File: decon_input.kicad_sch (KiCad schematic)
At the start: 35 parts, among them J21 Conn_01x02, U1 LTV-817S, U2 LTV-817S, U22 LTV-817S, U23 LTV-817S, U24 LTV-817S, U25 LTV-817S, U4 LTV-817S, U5 LTV-817S

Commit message: modified:   DECON_Ctrl_Panel.kicad_pcb 	modified:   DECON_Ctrl_Panel.kicad_prl 	new file:   MCU_pins.xlsx 	new file:   Son_KiCad_lib/Son_KiCad_lib.bak 	new file:   Son_KiCad_lib/Son_KiCad_lib.kicad_sym 	new file:   Son_KiCad_lib/Son_KiCad_lib.pretty/URB2405YMD-10WR3.kicad_mod 	modified:   decon_input.kicad_sch 	modified:   decon_mcu.kicad_sch 	modified:   decon_output.kicad_sch 	modified:   decon_power.kicad_sch 	new file:   fp-lib-table 	new file:   sym-lib-table
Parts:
- removed D1, D2, D3, D4, D41, D5, D6, D7: LED, LED_SMD:LED_0805_2012Metric, symbol Device:LED
- removed J21: Conn_01x02, TerminalBlock_Phoenix:TerminalBlock_Phoenix_MKDS-1-2-3.81_1x02_P3.81mm_Horizontal, symbol Connector_Generic:Conn_01x02
- removed R1, R3, R41, R45, R5, R7: 1K, Resistor_SMD:R_0805_2012Metric, symbol Device:R
- removed R2, R4, R42, R46, R6, R8: 10K, Resistor_SMD:R_0805_2012Metric, symbol Device:R
- removed U1, U2, U22, U23, U24, U25, U4, U5: LTV-817S, Package_DIP:SMDIP-4_W9.53mm, symbol Isolator:LTV-817S
- added J21, J22: Conn_01x10, Connector_Phoenix_MC:PhoenixContact_MC_1,5_10-G-3.81_1x10_P3.81mm_Horizontal, symbol Connector_Generic:Conn_01x10
- added R51, R52, R53, R54, R71, R72, R73, R74, R75, R76: 1K, Resistor_SMD:R_0805_2012Metric, symbol Device:R
- added R65, R66, R67, R68, R69, R70, R77, R78, R79, R80, R81, R82, R83, R84, R85, R86, R87, R88, R89: 10K, Resistor_SMD:R_0805_2012Metric, symbol Device:R
- added U2: 74HC138, Package_SO:SOIC-16_3.9x9.9mm_P1.27mm, symbol 74xx:74HC138
- added U26, U27, U34, U35, U36, U37, U38, U39: LTV-817S, Package_DIP:SMDIP-4_W9.53mm, symbol Isolator:LTV-817S
- R48, R50: value 10K -> 1K
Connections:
- net 24V is gone; now on net 3.3V: R43.1
- net BUTTON_1 is gone; now on net 3.3V: R47.1, R49.1
- net 3.3V: now also R44.1, R51.1, R53.1, R65.2, R66.2, R67.2, R68.2, R69.2, R70.2, R77.2, R78.2, R79.2, R80.2, R81.2, R82.2, R83.2, R84.2, R85.2, R86.2, R87.2, R88.2, R89.2, U2.16 (VCC), U2.6 (E2)
- net at R47.2: now also U34.1
- net at R49.2: now also U36.1
- net at R48.2: now also U35.1
- net at R43.2: now also U26.1; no longer R44.1
- net at R50.2: now also U37.1
- net GND_24V: no longer names the net of R44.2
- net GND_24V: now also U27.1
- new net: R52.1, U26.4
- new net: R71.1, U34.4
- new net: R51.2, U38.1
- new net: R53.2, U39.1
- new net: R76.1, U39.4
- new net: R73.1, U36.4
- new net: R54.1, U27.4
- new net: R72.1, U35.4
- new net: R74.1, U37.4
- new net: R75.1, U38.4
- new net 74138_Y0: R65.1, R89.1, U2.15 (~{Y0}), U2.3 (A2), U26.2
- new net 74138_Y1: R66.1, R88.1, U2.14 (~{Y1}), U2.2 (A1), U34.2
- new net 74138_Y2: R67.1, R87.1, U2.1 (A0), U2.13 (~{Y2}), U35.2
- new net 74138_Y3: R68.1, U2.12 (~{Y3}), U36.2
- new net 74138_Y4: R69.1, U2.11 (~{Y4}), U27.2
- new net 74138_Y5: R70.1, U2.10 (~{Y5}), U37.2
- new net 74138_Y6: R77.1, U2.9 (~{Y6}), U38.2
- new net 74138_Y7: R78.1, U2.7 (~{Y7}), U39.2
- new net GND_MCU: J21.1 (Pin_1), J21.10 (Pin_10), U2.4 (~{E0}), U2.5 (~{E1}), U2.8 (GND)
- new net GND_VBAT: J22.1 (Pin_1), J22.10 (Pin_10)
- new net LED_0: U26.3
- new net LED_1: J22.2 (Pin_2), U34.3
- new net LED_2: J22.3 (Pin_3), U35.3
- new net LED_3: J22.4 (Pin_4), U36.3
- new net LED_4: J22.5 (Pin_5), U27.3
- new net LED_5: J22.6 (Pin_6), U37.3
- new net LED_6: J22.7 (Pin_7), U38.3
- new net LED_7: J22.8 (Pin_8), U39.3
- new net LED_8: J22.9 (Pin_9)
- new net MCU_BTN_0: J21.2 (Pin_2), R86.1
- new net MCU_BTN_1: J21.3 (Pin_3), R85.1
- new net MCU_BTN_2: J21.4 (Pin_4), R84.1
- new net MCU_BTN_3: J21.5 (Pin_5), R83.1
- new net MCU_BTN_4: J21.6 (Pin_6), R82.1
- new net MCU_BTN_5: J21.7 (Pin_7), R81.1
- new net MCU_BTN_6: J21.8 (Pin_8), R80.1
- new net MCU_BTN_7: J21.9 (Pin_9), R79.1
- new net VBAT: R52.2, R54.2, R71.2, R72.2, R73.2, R74.2, R75.2, R76.2

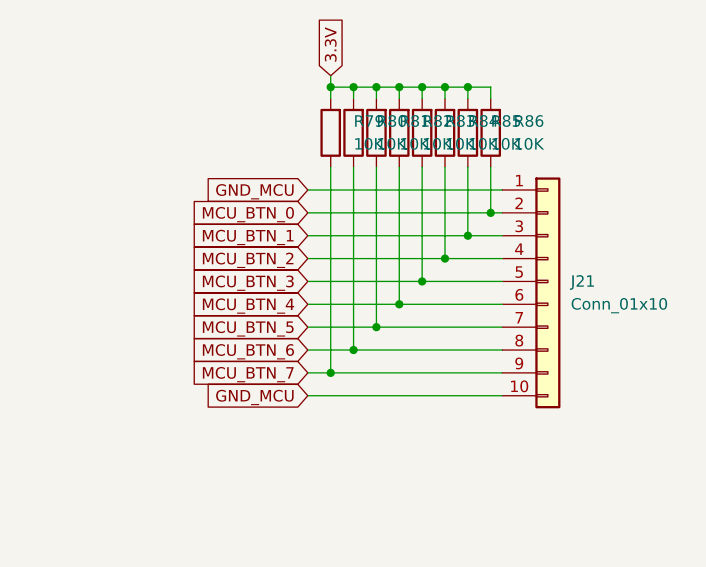
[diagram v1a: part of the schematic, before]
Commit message: modified:   DECON_Ctrl_Panel.kicad_sch
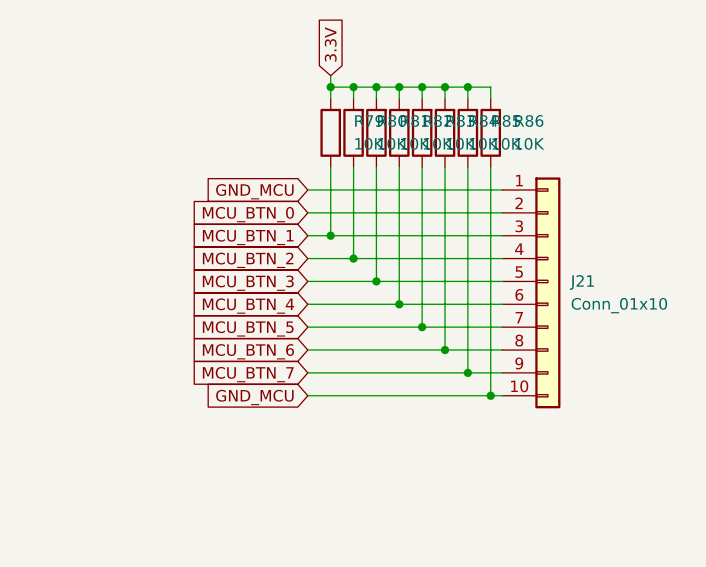
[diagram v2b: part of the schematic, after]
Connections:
- net GND_MCU: now also R86.1
- net MCU_BTN_0: no longer R86.1
- net MCU_BTN_1: now also R79.1; no longer R85.1
- net MCU_BTN_2: now also R80.1; no longer R84.1
- net MCU_BTN_3: now also R81.1; no longer R83.1
- net MCU_BTN_5: now also R83.1; no longer R81.1
- net MCU_BTN_6: now also R84.1; no longer R80.1
- net MCU_BTN_7: now also R85.1; no longer R79.1
